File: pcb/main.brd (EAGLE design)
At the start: 160 x 100 mm, 34 parts, among them IC1 FT230XS, J3 455-1750-1-ND, J6 M1 connector, J7 M2 connector, Q1 2.5A/30V/105mΩ

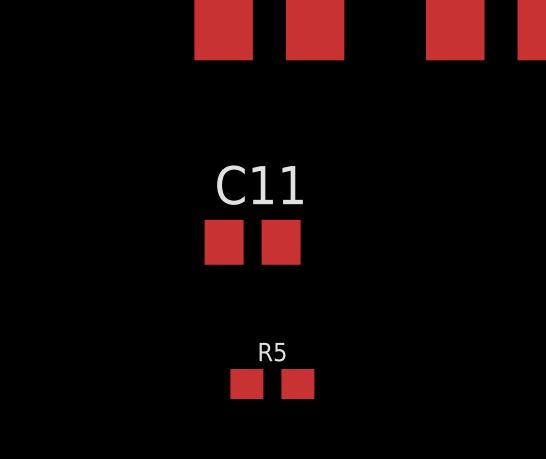
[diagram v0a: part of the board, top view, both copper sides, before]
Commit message: added IMU
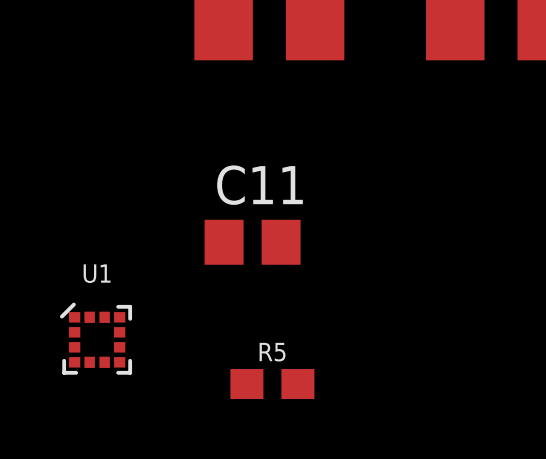
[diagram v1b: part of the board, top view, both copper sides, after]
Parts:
- added U1: LSM303C, SparkFun-Sensors:LGA-12
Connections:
- new net SCL: U1.1
- new net SDA: U1.4
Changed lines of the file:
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@@
 <attribute name="PROD_ID" value=" " x="-64.0588" y="-101.092" size="1.778" layer="27" display="off"/>
+</element>
+<element name="U1" library="SparkFun-Sensors" library_urn="urn:adsk.eagle:library:534" package="LGA-12" package3d_urn="urn:adsk.eagle:package:39983/1" value="LSM303C" x="-69.9008" y="-99.6188">
+<attribute name="PROD_ID" value="IC-12557" x="-69.9008" y="-99.6188" size="1.778" layer="27" display="off"/>
 </element>
 </elements>
@@
 <wire x1="-29.475" y1="38.985" x2="-64.9088" y2="-101.092" width="0" layer="19" extent="1-1"/>
 </signal>
+<signal name="SCL">
+<contactref element="U1" pad="1"/>
+</signal>
+<signal name="SDA">
+<contactref element="U1" pad="4"/>
+</signal>
 </signals>

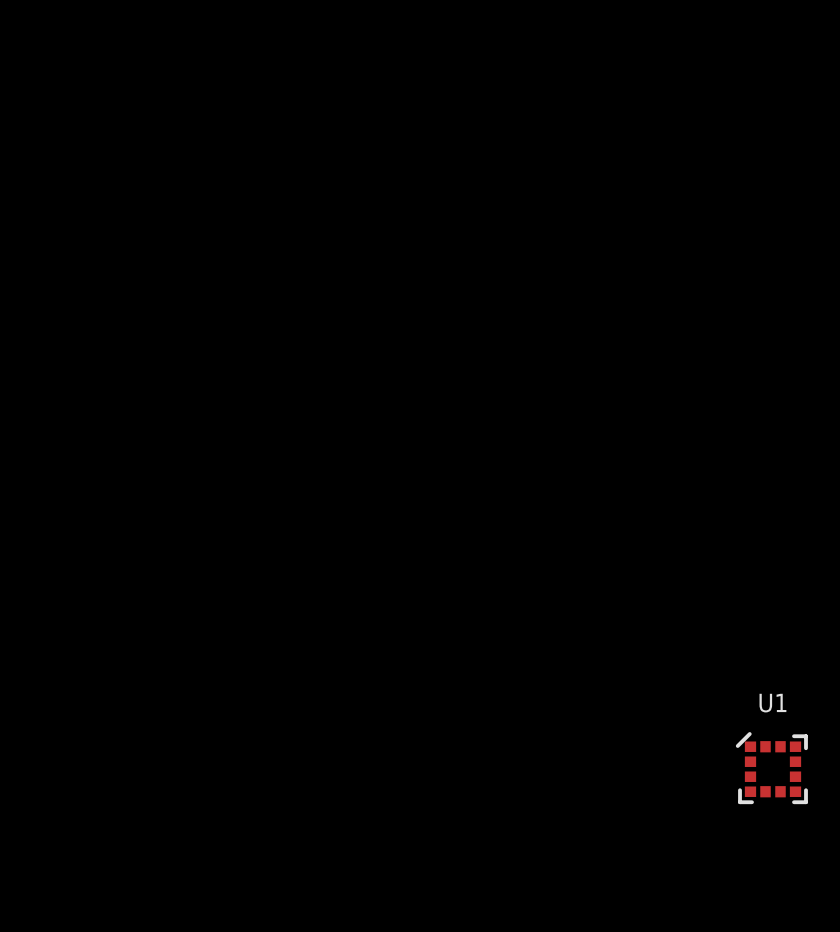
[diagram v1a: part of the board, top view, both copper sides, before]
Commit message: changed gnd symbol (some weird 3.3v thing was happening) and added esp32
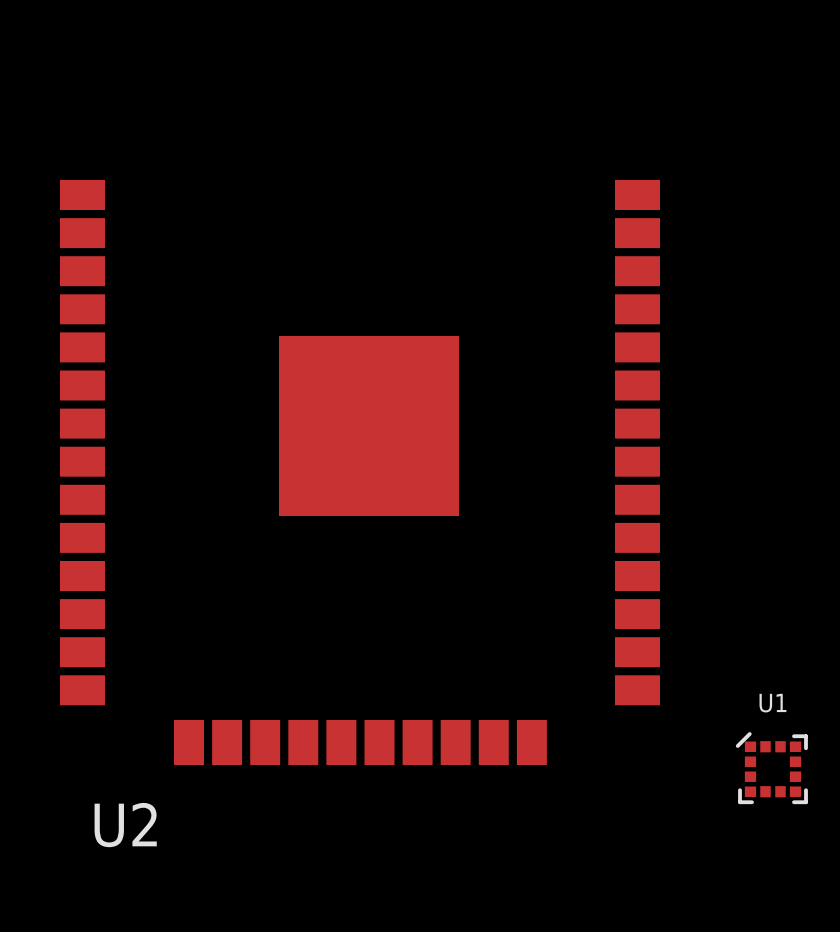
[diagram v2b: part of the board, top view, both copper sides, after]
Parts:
- added U2: ESP-WROOM-32, electricSheepParty:ESP-WROOM-32
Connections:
- removed net N$10: C10.-, C11.2, C6.2, C7.2, C8.2, C9.-, D3.1, U$3.3, U$3.5, U$3.6
- removed net N$6: C3.2, C4.2, U$2.13, U$2.17
- net 3V3: now also U2.2
- net GND: now also C10.-, C11.2, C3.2, C4.2, C6.2, C7.2, C8.2, C9.-, D3.1, U$2.13, U$2.17, U$3.3, U$3.5, U$3.6, U2.1, U2.15, U2.38, U2.GND
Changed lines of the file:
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@@
 <?xml version="1.0" encoding="utf-8"?>
 <!DOCTYPE eagle SYSTEM "eagle.dtd">
-<eagle version="8.3.2">
+<eagle version="8.5.2">
 <drawing>
 <settings>
@@
 <layer number="59" name="tCarbon" color="7" fill="1" visible="no" active="no"/>
 <layer number="60" name="bCarbon" color="7" fill="1" visible="no" active="no"/>
-<layer number="88" name="SimResults" color="9" fill="1" visible="yes" active="yes"/>
-<layer number="89" name="SimProbes" color="9" fill="1" visible="yes" active="yes"/>
+<layer number="88" name="SimResults" color="9" fill="1" visible="no" active="no"/>
+<layer number="89" name="SimProbes" color="9" fill="1" visible="no" active="no"/>
 <layer number="90" name="Modules" color="5" fill="1" visible="no" active="no"/>
 <layer number="91" name="Nets" color="2" fill="1" visible="no" active="no"/>
@@
 <param name="dpMaxLengthDifference" value="10mm"/>
 <param name="dpGapFactor" value="2.5"/>
-<param name="checkGrid" value="0"/>
 <param name="checkAngle" value="0"/>
 <param name="checkFont" value="1"/>
 <param name="checkRestrict" value="1"/>
+<param name="checkStop" value="0"/>
+<param name="checkValues" value="0"/>
 <param name="useDiameter" value="13"/>
 <param name="maxErrors" value="50"/>
@@
 <attribute name="PROD_ID" value="IC-12557" x="-69.9008" y="-99.6188" size="1.778" layer="27" display="off"/>
 </element>
+<element name="U2" library="electricSheepParty" package="ESP-WROOM-32" value="ESP-WROOM-32" x="-83.6676" y="-87.4776"/>
 </elements>
 <signals>
@@
 <contactref element="U$2" pad="6"/>
 <contactref element="U$2" pad="3"/>
-<wire x1="-19.9" y1="54.61" x2="-14.39" y2="54.61" width="0" layer="19" extent="1-1"/>
-<wire x1="-17.78" y1="49.53" x2="-19.9" y2="54.61" width="0" layer="19" extent="1-1"/>
-<wire x1="-24.13" y1="49.53" x2="-17.78" y2="49.53" width="0" layer="19" extent="1-1"/>
-<wire x1="-30.48" y1="49.53" x2="-24.13" y2="49.53" width="0" layer="19" extent="1-1"/>
+<contactref element="U2" pad="15"/>
+<contactref element="U2" pad="GND"/>
+<contactref element="U2" pad="38"/>
+<contactref element="U$2" pad="17"/>
+<contactref element="U$2" pad="13"/>
+<contactref element="C3" pad="2"/>
+<contactref element="C4" pad="2"/>
+<contactref element="U2" pad="1"/>
+<contactref element="D3" pad="1"/>
+<contactref element="U$3" pad="3"/>
+<contactref element="U$3" pad="6"/>
+<contactref element="U$3" pad="5"/>
+<contactref element="C7" pad="2"/>
+<contactref element="C6" pad="2"/>
+<contactref element="C8" pad="2"/>
+<contactref element="C9" pad="-"/>
+<contactref element="C10" pad="-"/>
+<contactref element="C11" pad="2"/>
+<wire x1="-83.3676" y1="-88.1776" x2="-89.3676" y2="-98.7276" width="0" layer="19" extent="1-1"/>
+<wire x1="-74.4176" y1="-80.4776" x2="-83.3676" y2="-88.1776" width="0" layer="19" extent="1-1"/>
+<wire x1="-65.6854" y1="-89.0524" x2="-74.4176" y2="-80.4776" width="0" layer="19" extent="1-1"/>
+<wire x1="-63.7692" y1="-96.3676" x2="-65.6854" y2="-89.0524" width="0" layer="19" extent="1-1"/>
+<wire x1="-57.9638" y1="-89.0524" x2="-65.6854" y2="-89.0524" width="0" layer="19" extent="1-1"/>
+<wire x1="-48.326" y1="-86.9696" x2="-57.9638" y2="-89.0524" width="0" layer="19" extent="1-1"/>
+<wire x1="-47.7656" y1="-91.694" x2="-48.326" y2="-86.9696" width="0" layer="19" extent="1-1"/>
+<wire x1="-48.326" y1="-81.3308" x2="-48.326" y2="-86.9696" width="0" layer="19" extent="1-1"/>
+<wire x1="-49.8196" y1="-75.6236" x2="-48.326" y2="-81.3308" width="0" layer="19" extent="1-1"/>
+<wire x1="-92.9176" y1="-80.4776" x2="-83.3676" y2="-88.1776" width="0" layer="19" extent="1-1"/>
+<wire x1="-47.41" y1="-12.7" x2="-49.8196" y2="-75.6236" width="0" layer="19" extent="1-1"/>
+<wire x1="-47.41" y1="-7.62" x2="-47.41" y2="-12.7" width="0" layer="19" extent="1-1"/>
+<wire x1="-39.5478" y1="27.6225" x2="-47.41" y2="-7.62" width="0" layer="19" extent="1-1"/>
+<wire x1="-34.1122" y1="28.2575" x2="-39.5478" y2="27.6225" width="0" layer="19" extent="1-1"/>
+<wire x1="-32.725" y1="38.985" x2="-34.1122" y2="28.2575" width="0" layer="19" extent="1-1"/>
+<wire x1="-30.775" y1="38.985" x2="-32.725" y2="38.985" width="0" layer="19" extent="1-1"/>
+<wire x1="-31.75" y1="41.91" x2="-32.725" y2="38.985" width="0" layer="19" extent="1-1"/>
+<wire x1="-32.075" y1="44.835" x2="-31.75" y2="41.91" width="0" layer="19" extent="1-1"/>
+<wire x1="-36.83" y1="40.64" x2="-32.725" y2="38.985" width="0" layer="19" extent="1-1"/>
+<wire x1="-30.48" y1="49.53" x2="-32.075" y2="44.835" width="0" layer="19" extent="1-1"/>
 <wire x1="-33.413" y1="53.34" x2="-30.48" y2="49.53" width="0" layer="19" extent="1-1"/>
 <wire x1="-36.83" y1="49.53" x2="-33.413" y2="53.34" width="0" layer="19" extent="1-1"/>
-<wire x1="-36.83" y1="40.64" x2="-36.83" y2="49.53" width="0" layer="19" extent="1-1"/>
-<wire x1="-32.725" y1="38.985" x2="-36.83" y2="40.64" width="0" layer="19" extent="1-1"/>
-<wire x1="-30.775" y1="38.985" x2="-32.725" y2="38.985" width="0" layer="19" extent="1-1"/>
+<wire x1="-24.13" y1="49.53" x2="-30.48" y2="49.53" width="0" layer="19" extent="1-1"/>
+<wire x1="-17.78" y1="49.53" x2="-24.13" y2="49.53" width="0" layer="19" extent="1-1"/>
+<wire x1="-19.9" y1="54.61" x2="-17.78" y2="49.53" width="0" layer="19" extent="1-1"/>
+<wire x1="-14.39" y1="54.61" x2="-19.9" y2="54.61" width="0" layer="19" extent="1-1"/>
 <wire x1="-46.14" y1="49.53" x2="-36.83" y2="49.53" width="0" layer="19" extent="1-1"/>
 <wire x1="-20.0914" y1="40.0812" x2="-17.78" y2="49.53" width="0" layer="19" extent="1-1"/>
-<wire x1="-34.1122" y1="28.2575" x2="-32.725" y2="38.985" width="0" layer="19" extent="1-1"/>
-<wire x1="-39.5478" y1="27.6225" x2="-34.1122" y2="28.2575" width="0" layer="19" extent="1-1"/>
+<wire x1="-21.59" y1="33.02" x2="-20.0914" y2="40.0812" width="0" layer="19" extent="1-1"/>
+<wire x1="-21.59" y1="23.12" x2="-21.59" y2="33.02" width="0" layer="19" extent="1-1"/>
+<wire x1="-18.19" y1="23.12" x2="-21.59" y2="23.12" width="0" layer="19" extent="1-1"/>
 </signal>
 <signal name="VCC">
@@
 <contactref element="R4" pad="2"/>
 </signal>
-<signal name="N$6">
-<contactref element="U$2" pad="17"/>
-<contactref element="U$2" pad="13"/>
-<contactref element="C3" pad="2"/>
-<contactref element="C4" pad="2"/>
-<wire x1="-47.41" y1="-7.62" x2="-47.41" y2="-12.7" width="0" layer="19" extent="1-1"/>
-<wire x1="-31.75" y1="41.91" x2="-47.41" y2="-7.62" width="0" layer="19" extent="1-1"/>
-<wire x1="-32.075" y1="44.835" x2="-31.75" y2="41.91" width="0" layer="19" extent="1-1"/>
-</signal>
 <signal name="3V3">
 <contactref element="R3" pad="2"/>
@@
 <contactref element="R5" pad="2"/>
 <contactref element="U$2" pad="1"/>
-<wire x1="-65.6692" y1="-96.3676" x2="-63.2088" y2="-101.092" width="0" layer="19" extent="1-1"/>
+<contactref element="U2" pad="2"/>
+<wire x1="-65.6692" y1="-96.3676" x2="-92.9176" y2="-81.7476" width="0" layer="19" extent="1-1"/>
+<wire x1="-63.2088" y1="-101.092" x2="-65.6692" y2="-96.3676" width="0" layer="19" extent="1-1"/>
 <wire x1="-62.6354" y1="-89.0524" x2="-65.6692" y2="-96.3676" width="0" layer="19" extent="1-1"/>
 <wire x1="-54.9138" y1="-89.0524" x2="-62.6354" y2="-89.0524" width="0" layer="19" extent="1-1"/>
@@
 <wire x1="-23.29" y1="23.12" x2="-46.1264" y2="-60.2436" width="0" layer="19" extent="1-1"/>
 </signal>
-<signal name="N$10">
-<contactref element="D3" pad="1"/>
-<contactref element="U$3" pad="3"/>
-<contactref element="U$3" pad="6"/>
-<contactref element="U$3" pad="5"/>
-<contactref element="C7" pad="2"/>
-<contactref element="C6" pad="2"/>
-<contactref element="C8" pad="2"/>
-<contactref element="C9" pad="-"/>
-<contactref element="C10" pad="-"/>
-<contactref element="C11" pad="2"/>
-<wire x1="-65.6854" y1="-89.0524" x2="-63.7692" y2="-96.3676" width="0" layer="19" extent="1-1"/>
-<wire x1="-57.9638" y1="-89.0524" x2="-65.6854" y2="-89.0524" width="0" layer="19" extent="1-1"/>
-<wire x1="-48.326" y1="-86.9696" x2="-57.9638" y2="-89.0524" width="0" layer="19" extent="1-1"/>
-<wire x1="-47.7656" y1="-91.694" x2="-48.326" y2="-86.9696" width="0" layer="19" extent="1-1"/>
-<wire x1="-48.326" y1="-81.3308" x2="-48.326" y2="-86.9696" width="0" layer="19" extent="1-1"/>
-<wire x1="-49.8196" y1="-75.6236" x2="-48.326" y2="-81.3308" width="0" layer="19" extent="1-1"/>
-<wire x1="-21.59" y1="23.12" x2="-49.8196" y2="-75.6236" width="0" layer="19" extent="1-1"/>
-<wire x1="-18.19" y1="23.12" x2="-21.59" y2="23.12" width="0" layer="19" extent="1-1"/>
-<wire x1="-21.59" y1="33.02" x2="-21.59" y2="23.12" width="0" layer="19" extent="1-1"/>
-</signal>
 <signal name="6V">

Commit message: added in new gnd symbols (doesn't default to 3.3v anymore); added in esp32 library
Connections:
- net 3V3: no longer U2.2
- net VCC: now also U2.2
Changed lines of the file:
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@@
 <contactref element="Q1" pad="2"/>
 <contactref element="S1" pad="P$2"/>
+<contactref element="U2" pad="2"/>
+<wire x1="-29.21" y1="11.43" x2="-92.9176" y2="-81.7476" width="0" layer="19" extent="1-1"/>
+<wire x1="-34.1122" y1="27.6225" x2="-29.21" y2="11.43" width="0" layer="19" extent="1-1"/>
+<wire x1="-24.45" y1="40.91" x2="-34.1122" y2="27.6225" width="0" layer="19" extent="1-1"/>
+<wire x1="-15.24" y1="49.53" x2="-24.45" y2="40.91" width="0" layer="19" extent="1-1"/>
 <wire x1="-22.01" y1="54.61" x2="-15.24" y2="49.53" width="0" layer="19" extent="1-1"/>
-<wire x1="-24.45" y1="40.91" x2="-15.24" y2="49.53" width="0" layer="19" extent="1-1"/>
-<wire x1="-34.1122" y1="27.6225" x2="-24.45" y2="40.91" width="0" layer="19" extent="1-1"/>
-<wire x1="-29.21" y1="11.43" x2="-34.1122" y2="27.6225" width="0" layer="19" extent="1-1"/>
 <wire x1="-43.06" y1="49.53" x2="-24.45" y2="40.91" width="0" layer="19" extent="1-1"/>
 </signal>
@@
 <contactref element="R5" pad="2"/>
 <contactref element="U$2" pad="1"/>
-<contactref element="U2" pad="2"/>
-<wire x1="-65.6692" y1="-96.3676" x2="-92.9176" y2="-81.7476" width="0" layer="19" extent="1-1"/>
-<wire x1="-63.2088" y1="-101.092" x2="-65.6692" y2="-96.3676" width="0" layer="19" extent="1-1"/>
+<wire x1="-65.6692" y1="-96.3676" x2="-63.2088" y2="-101.092" width="0" layer="19" extent="1-1"/>
 <wire x1="-62.6354" y1="-89.0524" x2="-65.6692" y2="-96.3676" width="0" layer="19" extent="1-1"/>
 <wire x1="-54.9138" y1="-89.0524" x2="-62.6354" y2="-89.0524" width="0" layer="19" extent="1-1"/>

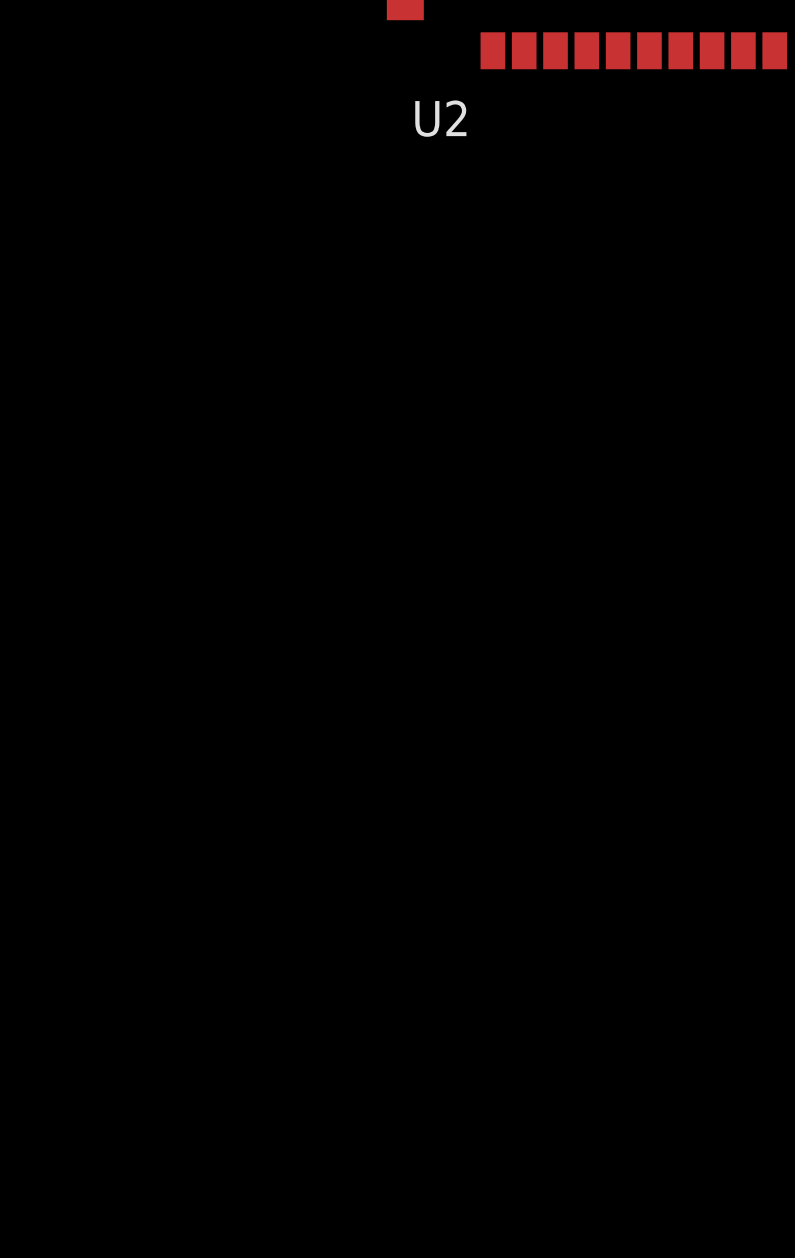
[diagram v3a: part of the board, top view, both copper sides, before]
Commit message: Did IMU and most of UART
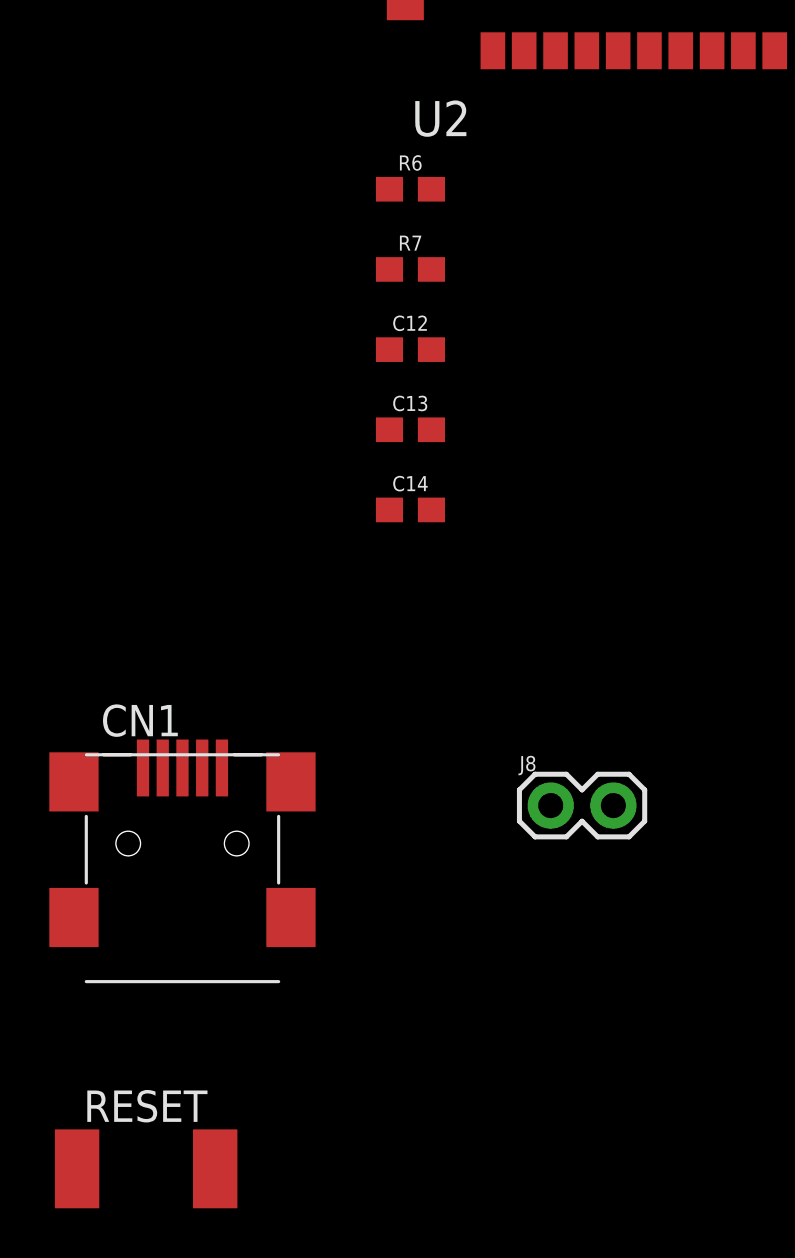
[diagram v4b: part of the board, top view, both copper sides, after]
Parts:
- added C12, C13: 0.1uF, electricSheepParty:0603
- added C14: 10uF, electricSheepParty:0603
- added CN1: (no value), adafruit:USB-MINIB
- added FRAME2: FRAME-LETTERNO_PACKAGE, SparkFun-Aesthetics:DUMMY
- added J8: (no value), electricSheepParty:1X02
- added R6, R7: 10k, electricSheepParty:0603
- added RESET: (no value), DiscreteComponents:SW_2512
- R1: value (none) -> 100k
- R2: value (none) -> 330
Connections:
- removed net VCCIO: IC1.3
- new net CTS: IC1.6
- new net D+: CN1.D+, IC1.8
- new net D-: CN1.D-, IC1.9
- new net INT_MAG: J8.1, U1.7
- new net INT_XL: J8.2, U1.12
- new net MAG_RDY: U1.11
- new net N$12: R6.2, R7.1, U1.2, U1.3
- new net N$6: C12.1, U1.5
- new net RESET: IC1.11, RESET.1
- new net RTS: IC1.2
- new net RX: IC1.4
- new net TX: IC1.1
- net 3V3: now also C13.1, C14.1, CN1.VBUS, IC1.10, IC1.12, IC1.3, R7.2, U1.10, U1.9, U2.2
- net GND: now also C12.2, C13.2, C14.2, CN1.GND, R6.1, RESET.2, U1.6, U1.8
- net VCC: no longer IC1.12, U2.2
